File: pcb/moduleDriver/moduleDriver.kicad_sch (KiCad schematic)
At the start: 31 parts, among them J1 UART_RL, J10 Sensor, J11 Power, J12 Power, J2 UART_LR, J3 MOTOR, J4 MOTOR, J5 MOTOR, J6 MOTOR, J7 Sensor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

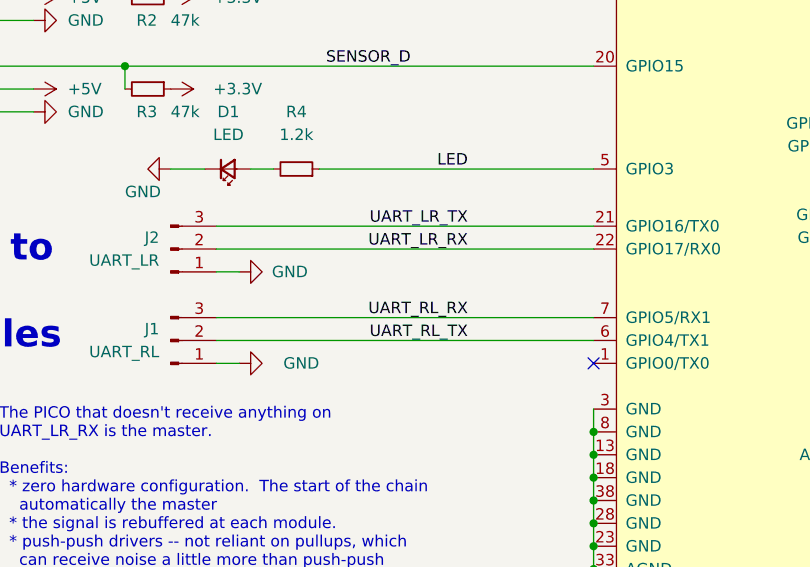
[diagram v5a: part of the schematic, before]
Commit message: Add serial resistors to uart
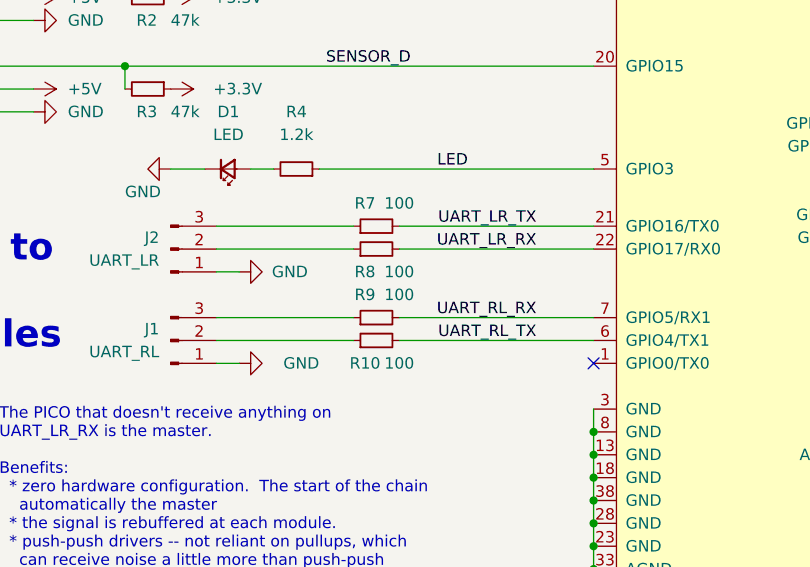
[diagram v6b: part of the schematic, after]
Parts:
- added R10, R7, R8, R9: 100, Resistor_SMD:R_0603_1608Metric, symbol Device:R_Small
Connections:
- net UART_LR_RX: now also R8.2; no longer J2.2 (Pin_2)
- net UART_LR_TX: now also R7.2; no longer J2.3 (Pin_3)
- net UART_RL_RX: now also R9.2; no longer J1.3 (Pin_3)
- net UART_RL_TX: now also R10.2; no longer J1.2 (Pin_2)
- new net: J1.2 (Pin_2), R10.1
- new net: J1.3 (Pin_3), R9.1
- new net: J2.2 (Pin_2), R8.1
- new net: J2.3 (Pin_3), R7.1
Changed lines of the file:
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@@
     (stroke (width 0) (type default) (color 0 0 0 0))
   )
-  (wire (pts (xy 60.96 106.68) (xy 102.87 106.68))
+  (wire (pts (xy 60.96 106.68) (xy 76.2 106.68))
     (stroke (width 0) (type default) (color 0 0 0 0))
   )
@@
     (stroke (width 0) (type default) (color 0 0 0 0))
   )
+  (wire (pts (xy 81.28 119.38) (xy 102.87 119.38))
+    (stroke (width 0) (type default) (color 0 0 0 0))
+  )
   (wire (pts (xy 215.9 107.95) (xy 254 107.95))
     (stroke (width 0) (type default) (color 0 0 0 0))
@@
     (stroke (width 0) (type default) (color 0 0 0 0))
   )
-  (wire (pts (xy 60.96 119.38) (xy 102.87 119.38))
+  (wire (pts (xy 60.96 119.38) (xy 76.2 119.38))
     (stroke (width 0) (type default) (color 0 0 0 0))
   )
@@
     (stroke (width 0) (type default) (color 0 0 0 0))
   )
-  (wire (pts (xy 60.96 116.84) (xy 102.87 116.84))
+  (wire (pts (xy 60.96 116.84) (xy 76.2 116.84))
     (stroke (width 0) (type default) (color 0 0 0 0))
   )
@@
     (stroke (width 0) (type default) (color 0 0 0 0))
   )
+  (wire (pts (xy 81.28 106.68) (xy 102.87 106.68))
+    (stroke (width 0) (type default) (color 0 0 0 0))
+  )
+  (wire (pts (xy 81.28 116.84) (xy 102.87 116.84))
+    (stroke (width 0) (type default) (color 0 0 0 0))
+  )
   (wire (pts (xy 215.9 102.87) (xy 254 102.87))
     (stroke (width 0) (type default) (color 0 0 0 0))
   )
+  (wire (pts (xy 81.28 109.22) (xy 102.87 109.22))
+    (stroke (width 0) (type default) (color 0 0 0 0))
+  )
   (wire (pts (xy 36.83 219.71) (xy 45.72 219.71))
     (stroke (width 0) (type default) (color 0 0 0 0))
   )
-  (wire (pts (xy 60.96 109.22) (xy 102.87 109.22))
+  (wire (pts (xy 60.96 109.22) (xy 76.2 109.22))
     (stroke (width 0) (type default) (color 0 0 0 0))
   )
@@
     (effects (font (size 1.27 1.27)) (justify right bottom))
   )
-  (label "UART_RL_RX" (at 88.9 116.84 180)
+  (label "UART_RL_RX" (at 96.52 116.84 180)
     (effects (font (size 1.27 1.27)) (justify right bottom))
   )
@@
     (effects (font (size 1.27 1.27)) (justify right bottom))
   )
-  (label "UART_RL_TX" (at 88.9 119.38 180)
+  (label "UART_RL_TX" (at 96.52 119.38 180)
     (effects (font (size 1.27 1.27)) (justify right bottom))
   )
@@
     (effects (font (size 1.27 1.27)) (justify right bottom))
   )
-  (label "UART_LR_TX" (at 88.9 106.68 180)
+  (label "UART_LR_TX" (at 96.52 106.68 180)
     (effects (font (size 1.27 1.27)) (justify right bottom))
   )
@@
     (effects (font (size 1.27 1.27)) (justify right bottom))
   )
-  (label "UART_LR_RX" (at 88.9 109.22 180)
+  (label "UART_LR_RX" (at 96.52 109.22 180)
     (effects (font (size 1.27 1.27)) (justify right bottom))
   )
@@
     (pin "1")
   )
+  (symbol (lib_id "Device:R_Small") (at 78.74 109.22 90) (unit 1)
+    (in_bom yes) (on_board yes)
+    (property "Reference" "R8" (id 0) (at 77.47 111.76 90))
+    (property "Value" "100" (id 1) (at 81.28 111.76 90))
+    (property "Footprint" "Resistor_SMD:R_0603_1608Metric" (id 2) (at 78.74 109.22 0)
+      (effects (font (size 1.27 1.27)) hide)
+    )
+    (property "Datasheet" "https://datasheet.lcsc.com/lcsc/2206010130_UNI-ROYAL-Uniroyal-Elec-0603WAF1000T5E_C22775.pdf" (id 3) (at 78.74 109.22 0)
+      (effects (font (size 1.27 1.27)) hide)
+    )
+    (property "Comment" "Basic" (id 4) (at 78.74 109.22 0)
+      (effects (font (size 1.27 1.27)) hide)
+    )
+    (property "LCSC#" "C22775" (id 5) (at 78.74 109.22 0)
+      (effects (font (size 1.27 1.27)) hide)
+    )
+    (pin "1")
+    (pin "2")
+  )
   (symbol (lib_id "power:GND") (at 63.5 111.76 90) (mirror x) (unit 1)
     (in_bom yes) (on_board yes)
@@
     (pin "1")
   )
+  (symbol (lib_id "Device:R_Small") (at 78.74 106.68 90) (unit 1)
+    (in_bom yes) (on_board yes)
+    (property "Reference" "R7" (id 0) (at 77.47 104.14 90))
+    (property "Value" "100" (id 1) (at 81.28 104.14 90))
+    (property "Footprint" "Resistor_SMD:R_0603_1608Metric" (id 2) (at 78.74 106.68 0)
+      (effects (font (size 1.27 1.27)) hide)
+    )
+    (property "Datasheet" "https://datasheet.lcsc.com/lcsc/2206010130_UNI-ROYAL-Uniroyal-Elec-0603WAF1000T5E_C22775.pdf" (id 3) (at 78.74 106.68 0)
+      (effects (font (size 1.27 1.27)) hide)
+    )
+    (property "Comment" "Basic" (id 4) (at 78.74 106.68 0)
+      (effects (font (size 1.27 1.27)) hide)
+    )
+    (property "LCSC#" "C22775" (id 5) (at 78.74 106.68 0)
+      (effects (font (size 1.27 1.27)) hide)
+    )
+    (pin "1")
+    (pin "2")
+  )
   (symbol (lib_id "power:GND") (at 195.58 81.28 270) (mirror x) (unit 1)
     (in_bom yes) (on_board yes)
@@
     (pin "1")
   )
+  (symbol (lib_id "Device:R_Small") (at 78.74 119.38 90) (unit 1)
+    (in_bom yes) (on_board yes)
+    (property "Reference" "R10" (id 0) (at 77.47 121.92 90))
+    (property "Value" "100" (id 1) (at 81.28 121.92 90))
+    (property "Footprint" "Resistor_SMD:R_0603_1608Metric" (id 2) (at 78.74 119.38 0)
+      (effects (font (size 1.27 1.27)) hide)
+    )
+    (property "Datasheet" "https://datasheet.lcsc.com/lcsc/2206010130_UNI-ROYAL-Uniroyal-Elec-0603WAF1000T5E_C22775.pdf" (id 3) (at 78.74 119.38 0)
+      (effects (font (size 1.27 1.27)) hide)
+    )
+    (property "Comment" "Basic" (id 4) (at 78.74 119.38 0)
+      (effects (font (size 1.27 1.27)) hide)
+    )
+    (property "LCSC#" "C22775" (id 5) (at 78.74 119.38 0)
+      (effects (font (size 1.27 1.27)) hide)
+    )
+    (pin "1")
+    (pin "2")
+  )
   (symbol (lib_id "power:+5V") (at 40.64 81.28 270) (mirror x) (unit 1)
     (in_bom yes) (on_board yes) (fields_autoplaced)
@@
     (pin "1")
   )
+  (symbol (lib_id "Device:R_Small") (at 78.74 116.84 90) (unit 1)
+    (in_bom yes) (on_board yes)
+    (property "Reference" "R9" (id 0) (at 77.47 114.3 90))
+    (property "Value" "100" (id 1) (at 81.28 114.3 90))
+    (property "Footprint" "Resistor_SMD:R_0603_1608Metric" (id 2) (at 78.74 116.84 0)
+      (effects (font (size 1.27 1.27)) hide)
+    )
+    (property "Datasheet" "https://datasheet.lcsc.com/lcsc/2206010130_UNI-ROYAL-Uniroyal-Elec-0603WAF1000T5E_C22775.pdf" (id 3) (at 78.74 116.84 0)
+      (effects (font (size 1.27 1.27)) hide)
+    )
+    (property "Comment" "Basic" (id 4) (at 78.74 116.84 0)
+      (effects (font (size 1.27 1.27)) hide)
+    )
+    (property "LCSC#" "C22775" (id 5) (at 78.74 116.84 0)
+      (effects (font (size 1.27 1.27)) hide)
+    )
+    (pin "1")
+    (pin "2")
+  )
   (symbol (lib_id "Device:R_Small") (at 53.34 81.28 270) (unit 1)
     (in_bom yes) (on_board yes)
@@
       (reference "R6") (unit 1) (value "2.2k") (footprint "Resistor_SMD:R_0603_1608Metric")
     )
+    (path "/99462255-72a9-43f4-9c1e-0abfd0c92352"
+      (reference "R7") (unit 1) (value "100") (footprint "Resistor_SMD:R_0603_1608Metric")
+    )
+    (path "/5e36cafd-3aa8-474a-823d-b92bc4628b52"
+      (reference "R8") (unit 1) (value "100") (footprint "Resistor_SMD:R_0603_1608Metric")
+    )
+    (path "/ee529aab-97ed-4375-ab27-d8653b887554"
+      (reference "R9") (unit 1) (value "100") (footprint "Resistor_SMD:R_0603_1608Metric")
+    )
+    (path "/b4d73550-8974-49ae-8ddd-c73fa4f073d7"
+      (reference "R10") (unit 1) (value "100") (footprint "Resistor_SMD:R_0603_1608Metric")
+    )
     (path "/4d9a4616-b5c1-468d-9830-58dc65bfac21"

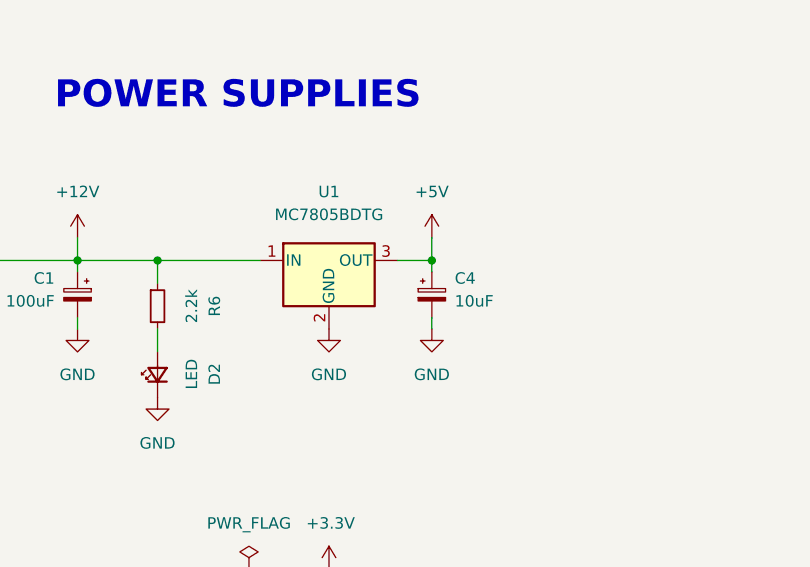
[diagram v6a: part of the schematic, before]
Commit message: Fix regulator caps
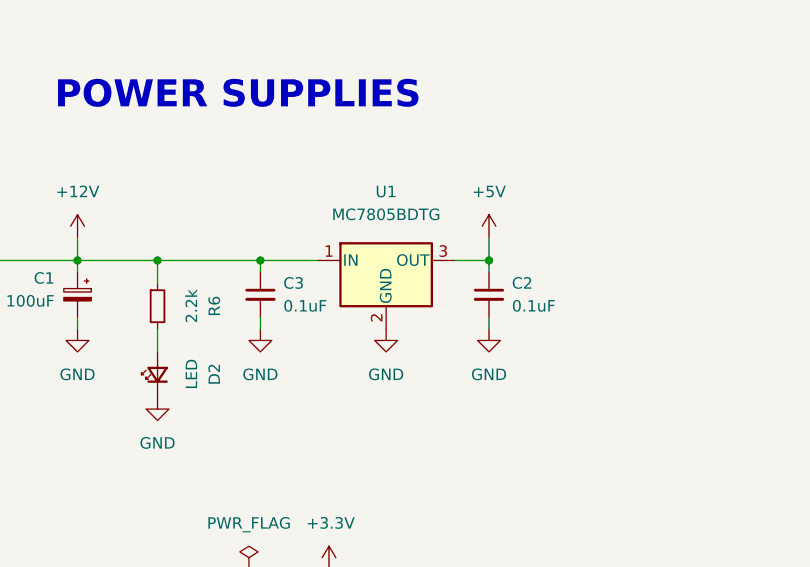
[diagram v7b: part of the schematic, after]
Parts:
- removed C4: 10uF, Capacitor_SMD:CP_Elec_4x5.3, symbol Device:C_Polarized_Small
- added C2, C3: 0.1uF, Capacitor_SMD:C_0603_1608Metric, symbol Device:C_Small
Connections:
- net +12V: now also C3.1
- net +5V: now also C2.1
- net GND: now also C2.2, C3.2
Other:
- moved on the sheet: U1

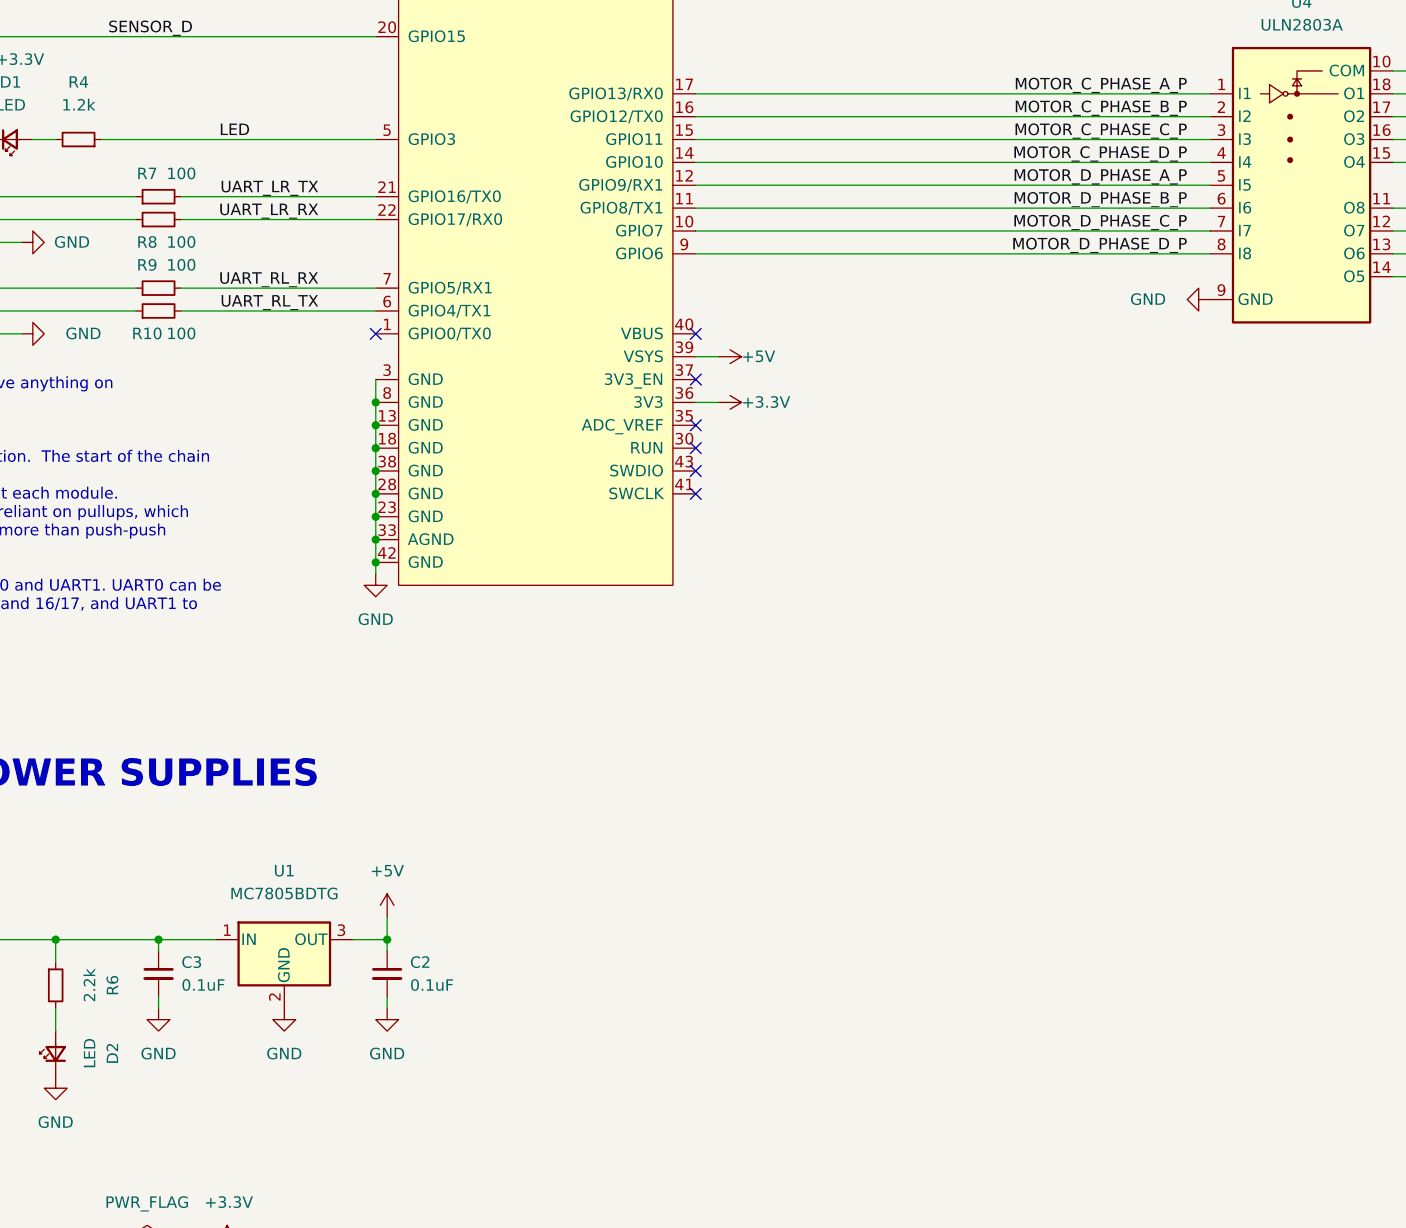
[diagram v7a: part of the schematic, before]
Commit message: Add support for neopixel
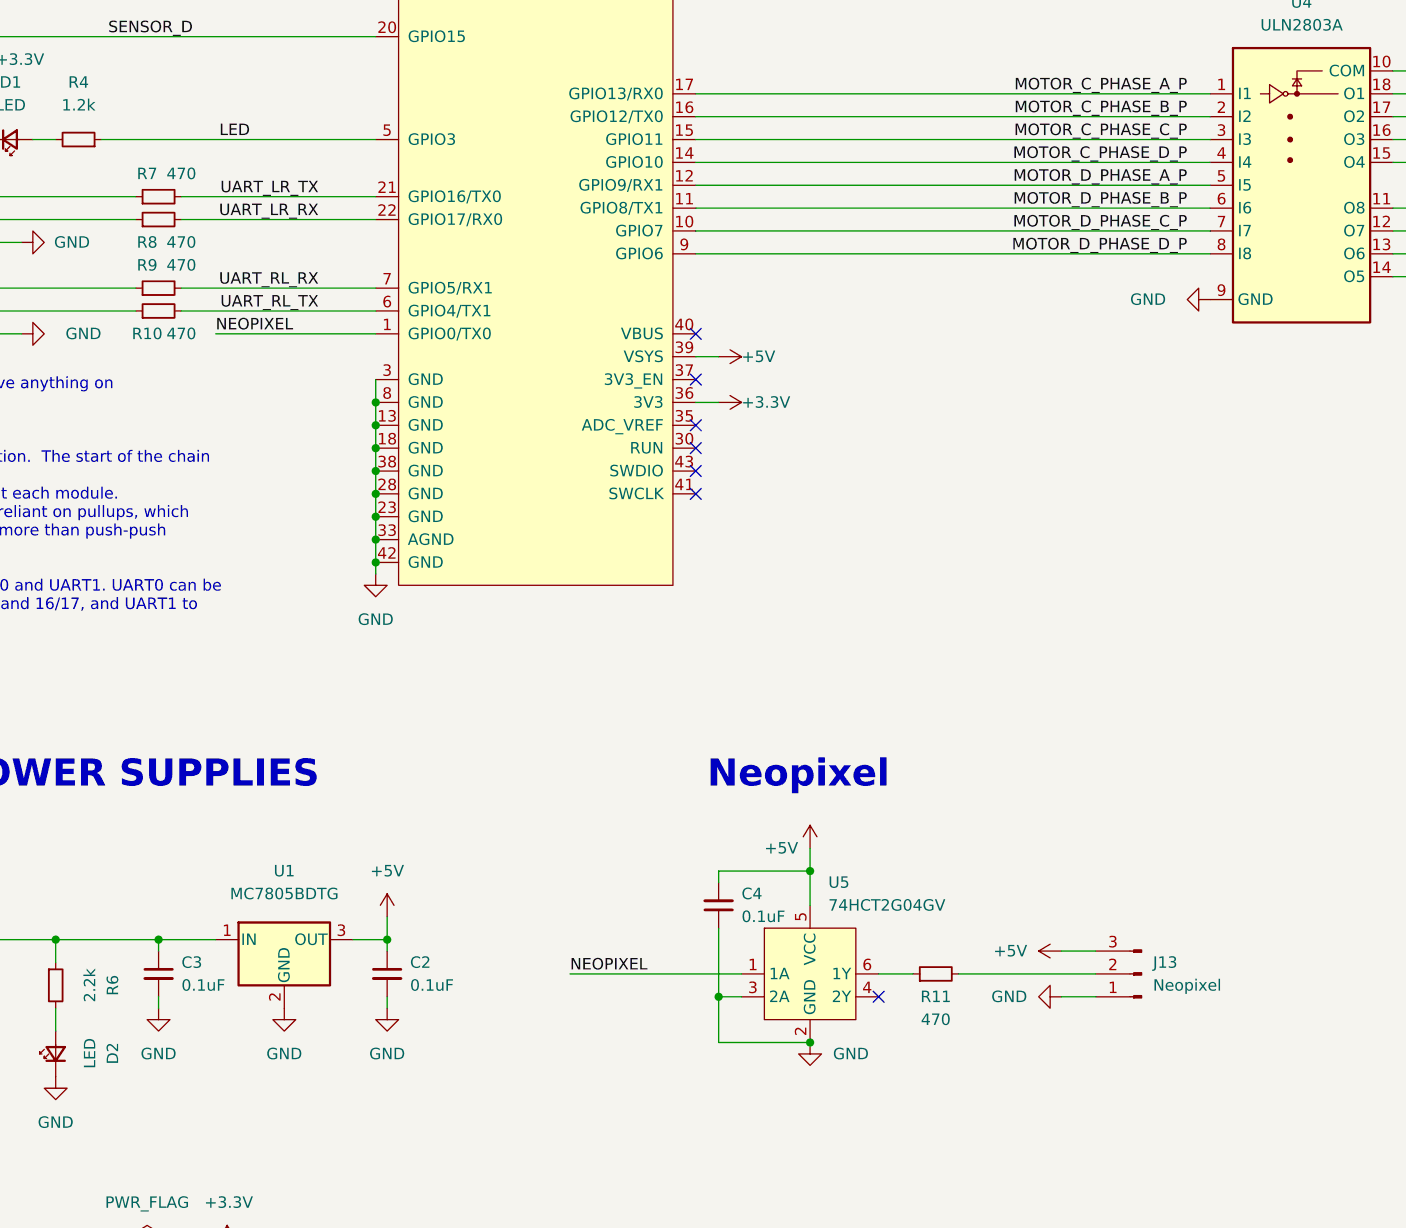
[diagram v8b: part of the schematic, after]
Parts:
- added C4: 0.1uF, Capacitor_SMD:C_0603_1608Metric, symbol Device:C_Small
- added J13: Neopixel, Connector_PinHeader_2.54mm:PinHeader_1x03_P2.54mm_Vertical, symbol Connector:Conn_01x03_Male
- added R11: 470, Resistor_SMD:R_0603_1608Metric, symbol Device:R_Small
- added U5: 74HCT2G04GV, Package_SO:SC-74-6_1.5x2.9mm_P0.95mm, symbol New_Library:74HCT2G04GV
- R10, R7, R8, R9: value 100 -> 470; LCSC# C22775 -> C23179
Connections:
- net +5V: now also C4.2, J13.3 (Pin_3), U5.5 (VCC)
- net GND: now also C4.1, J13.1 (Pin_1), U5.2 (GND), U5.3 (2A)
- net NEOPIXEL: now reaches U2.1 (GPIO0/TX0)
- net NEOPIXEL: now also U5.1 (1A)
- new net: R11.1, U5.6 (1Y)
- new net: J13.2 (Pin_2), R11.2
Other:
- note added: "Neopixel"
